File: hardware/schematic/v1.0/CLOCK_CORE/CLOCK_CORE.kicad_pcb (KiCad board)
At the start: 4 copper layers, 70 x 70 mm, 137 parts, among them CN1 LAIL-PHC2_54-2P-01-XH-L, J1 Conn_Coaxial, J3 Conn_01x04_Socket, U1 OCXO_20x20mm, U2 OCXO_25.4x25.4mm, U3 TPS7A5201RPSR, U4 TPS7A5201RPSR, U5 LMK5B12204, U6 REF5040

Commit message: pcb update
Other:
- board text added: "+5V"
- board text added: "GND"

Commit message: pcb update
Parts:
- R20: value DNP -> 0
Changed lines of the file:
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@@
 			)
 		)
-		(property "Value" "DNP"
+		(property "Value" "0"
 			(at 0 1.65 0)
 			(layer "F.Fab")
@@
 			)
 		)
-		(attr smd)
+		(attr smd dnp)
 		(duplicate_pad_numbers_are_jumpers no)
 		(fp_line
@@
 			)
 		)
-		(attr smd)
+		(attr smd dnp)
 		(duplicate_pad_numbers_are_jumpers no)
 		(fp_rect

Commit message: sch and pcb update
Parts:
- C1, C10, C11, C13, C15, C19, C2, C20, C21, C25, C26, C27, C28, C29, C3, C30, C31, C32, C33, C34, C35, C36, C37, C38, C39, C4, C40, C41, C42, C43, C44, C45, C46, C47, C48, C49, C5, C50, C51, C52, C53, C54, C55, C59, C6, C7, C8, C9: footprint Capacitor_SMD:C_0402_1005Metric -> CLOCK_CORE:C_0402_1005Metric
- C12, C14, C18, C56, C57, C58: footprint Capacitor_SMD:C_0603_1608Metric -> CLOCK_CORE:C_0603_1608Metric
- C16, C17, C23, C24: footprint Capacitor_SMD:C_0805_2012Metric -> CLOCK_CORE:C_0805_2012Metric
- C22: footprint JLCImport:TAJB107M010RNJ -> CLOCK_CORE:TAJB107M010RNJ
- CN1: footprint JLCImport:LAIL-PHC2_54-2P-01-XH-L -> CLOCK_CORE:LAIL-PHC2_54-2P-01-XH-L
- D1, D2, D3, D4, D5: footprint LED_SMD:LED_0603_1608Metric -> CLOCK_CORE:LED_0603_1608Metric
- F1: footprint JLCImport:BSMD1206C-1300T -> CLOCK_CORE:BSMD1206C-1300T
- FB1, FB2, FB3, FB4, FB5, FB6, FB7: footprint Inductor_SMD:L_0603_1608Metric -> CLOCK_CORE:L_0603_1608Metric
- H1: footprint JLCImport:HX_PH254-01-03-Z-L11_5_PCB_PIN_HEADER -> CLOCK_CORE:HX_PH254-01-03-Z-L11_5_PCB_PIN_HEADER
- H2, H3, H4, H5: footprint MountingHole:MountingHole_3.2mm_M3_Pad -> CLOCK_CORE:MountingHole_3.2mm_M3_Pad
- J1: footprint Connector_Coaxial:SMA_Amphenol_132134-11_Vertical -> CLOCK_CORE:SMA_Amphenol_132134-11_Vertical
- J3: footprint Connector_PinHeader_2.54mm:PinHeader_1x04_P2.54mm_Vertical -> CLOCK_CORE:PinHeader_1x04_P2.54mm_Vertical
- R1, R10, R11, R12, R13, R14, R16, R17, R18, R2, R21, R22, R23, R24, R3, R30, R31, R32, R33, R34, R35, R36, R37, R38, R4, R5, R6, R7, R8, R9: footprint Resistor_SMD:R_0402_1005Metric -> CLOCK_CORE:R_0402_1005Metric
- R15: footprint Counter:3296W-1-103_C48997937 -> CLOCK_CORE:3296W-1-103_C48997937
- R19, R20, R39: footprint Resistor_SMD:R_0805_2012Metric -> CLOCK_CORE:R_0805_2012Metric
- R25, R26, R27, R28, R29: footprint Resistor_SMD:R_0603_1608Metric -> CLOCK_CORE:R_0603_1608Metric
- RF1, RF10, RF2, RF3, RF4, RF5, RF6, RF7, RF8, RF9: footprint JLCImport:KH-IPEX-K501-29 -> CLOCK_CORE:KH-IPEX-K501-29
- TP1, TP2: footprint TestPoint:TestPoint_Pad_D1.0mm -> CLOCK_CORE:TestPoint_Pad_D1.0mm
- U1: footprint JLCImport:OCXO_20x20mm -> CLOCK_CORE:OCXO_20x20mm
- U2: footprint JLCImport:DOPFITKR2-10M -> CLOCK_CORE:DOPFITKR2-10M
- U3, U4: footprint JLCImport:TPS7A5201RPSR -> CLOCK_CORE:TPS7A5201RPSR
- U5: footprint Package_DFN_QFN:VQFN-48-1EP_7x7mm_P0.5mm_EP5.15x5.15mm_ThermalVias -> CLOCK_CORE:VQFN-48-1EP_7x7mm_P0.5mm_EP5.15x5.15mm_ThermalVias
- U6: footprint JLCImport:REF5040 -> CLOCK_CORE:REF5040

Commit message: sch and pcb update
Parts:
- R12, R3, R6, R9: value DNP -> 100
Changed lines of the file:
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@@
 			)
 		)
-		(property "Value" "DNP"
+		(property "Value" "100"
 			(at 0 1.17 90)
 			(layer "F.Fab")
@@
 			)
 		)
-		(property "Value" "DNP"
+		(property "Value" "100"
 			(at 0 1.17 90)
 			(layer "F.Fab")
@@
 			)
 		)
-		(property "Value" "DNP"
+		(property "Value" "100"
 			(at 0 1.17 90)
 			(layer "F.Fab")
@@
 			)
 		)
-		(property "Value" "DNP"
+		(property "Value" "100"
 			(at 0 1.17 90)
 			(layer "F.Fab")

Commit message: pcb update
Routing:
- net GND: track 111.1 -> 115.1 mm
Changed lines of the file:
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@@
+	)
+	(segment
+		(start 136.89 98.89)
+		(end 135.56 98.89)
+		(width 0.3)
+		(layer "F.Cu")
+		(net "GND")
 	)
 	(segment
@@
 	)
 	(segment
-		(start 136.89 98.89)
-		(end 136.89 99.64)
-		(width 0.3)
-		(layer "F.Cu")
-		(net "GND")
-	)
-	(segment
 		(start 179.2125 115.325)
 		(end 179.2125 116.15)
@@
 	)
 	(segment
+		(start 126.16 61.87)
+		(end 126.16 62.89)
+		(width 0.2)
+		(layer "F.Cu")
+		(net "GND")
+	)
+	(segment
 		(start 118.5 113.98)
 		(end 118.5 113.23)
@@
 	)
 	(segment
-		(start 126.1621 64.81)
-		(end 126.1621 64.06)
+		(start 126.1621 62.8921)
+		(end 126.1621 64.81)
 		(width 0.2)
 		(layer "F.Cu")
@@
 	)
 	(segment
+		(start 126.16 62.89)
+		(end 126.1621 62.8921)
+		(width 0.2)
+		(layer "F.Cu")
+		(net "GND")
+	)
+	(segment
 		(start 118.5 94.52)
 		(end 118.5 95.27)
@@
 	)
 	(via
-		(at 136.89 99.64)
+		(at 135.56 98.89)
 		(size 0.6)
 		(drill 0.3)
@@
 	)
 	(via
-		(at 126.1621 64.06)
-		(size 0.6)
-		(drill 0.3)
-		(layers "F.Cu" "B.Cu")
-		(net "GND")
-	)
-	(via
-		(at 150.1375 93.2975)
+		(at 126.16 61.87)
+		(size 0.6)
+		(drill 0.3)
+		(layers "F.Cu" "B.Cu")
+		(net "GND")
+	)
+	(via
+		(at 150.14 92.07)
 		(size 0.6)
 		(drill 0.3)
@@
 	)
 	(segment
+		(start 150.1375 94.0975)
+		(end 150.1375 92.0725)
+		(width 0.3)
+		(layer "B.Cu")
+		(net "GND")
+	)
+	(segment
 		(start 146.16 94.08)
 		(end 145.26 94.08)
@@
 	)
 	(segment
-		(start 150.1375 94.0975)
-		(end 150.1375 93.2975)
+		(start 150.1375 92.0725)
+		(end 150.14 92.07)
 		(width 0.3)
 		(layer "B.Cu")

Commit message: sch and pcb update
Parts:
- added R40: 0, CLOCK_CORE:R_0402_1005Metric, F.Cu at (165.4, 102.9)
- added R41: 0, CLOCK_CORE:R_0402_1005Metric, F.Cu at (165.4, 104.9)
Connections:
- R13 pad 1: OCXO_OUT -> OCXO_FR
- R30 pad 1: OCXO_OUT -> OCXO_FR
- U2 pad 1: OCXO_OUT -> OCXO_FR
- U5 pad 31: OCXO_OUT -> /LMK5B12204/OCXO_OUT
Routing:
- net OCXO_OUT: track 21.8 -> 0.00 mm
- net (no net): track 0.00 -> 21.8 mm

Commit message: sch and pcb update
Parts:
- moved R40 20.6 mm to (146.2, 95.6), turned to -90 degrees
- moved R41 19.8 mm to (147.6, 96.0)
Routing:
- net (no net): track 21.8 -> 0.00 mm
- net OCXO_FR: track 0.00 -> 16.7 mm
- net /LMK5B12204/OCXO_OUT: track 0.00 -> 5.00 mm
- net GND: track 115.1 -> 115.7 mm, vias 88 -> 87
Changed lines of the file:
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@@
 	(footprint "CLOCK_CORE:R_0402_1005Metric"
 		(layer "F.Cu")
-		(at 165.395 102.905)
+		(at 146.15 95.550001 -90)
 		(descr "Resistor SMD 0402 (1005 Metric), square (rectangular) end terminal, IPC-7351 nominal, (Body size source: IPC-SM-782 page 72, https://www.pcb-3d.com/wordpress/wp-content/uploads/ipc-sm-782a_amendment_1_and_2.pdf)")
 		(tags "resistor")
 		(property "Reference" "R40"
-			(at 0 -1.17 0)
+			(at 0.020001 -0.97 90)
 			(layer "F.SilkS")
+			(hide yes)
 			(effects
 				(font
-					(size 1 1)
-					(thickness 0.15)
+					(size 0.5 0.5)
+					(thickness 0.1)
+					(bold yes)
 				)
 			)
 		)
 		(property "Value" "0"
-			(at 0 1.17 0)
+			(at 0 1.17 90)
 			(layer "F.Fab")
+			(hide yes)
 			(effects
 				(font
@@
 		)
 		(property "Datasheet" ""
-			(at 0 0 0)
+			(at 0 0 90)
 			(layer "F.Fab")
 			(hide yes)
@@
 		)
 		(property "Description" ""
-			(at 0 0 0)
+			(at 0 0 90)
 			(layer "F.Fab")
 			(hide yes)
@@
 		)
 		(property "KiLib_Generator" "SMD_2terminal_chip_molded"
-			(at 0 0 0)
+			(at 0 0 90)
 			(layer "F.SilkS")
 			(hide yes)
@@
 		(duplicate_pad_numbers_are_jumpers no)
 		(fp_line
-			(start -0.153641 -0.38)
-			(end 0.153641 -0.38)
+			(start -0.153641 0.38)
+			(end 0.153641 0.38)
 			(stroke
 				(width 0.12)
@@
 		)
 		(fp_line
-			(start -0.153641 0.38)
-			(end 0.153641 0.38)
+			(start -0.153641 -0.38)
+			(end 0.153641 -0.38)
 			(stroke
 				(width 0.12)
@@
 			(layer "F.SilkS")
 		)
-		(fp_rect
-			(start -0.93 -0.47)
-			(end 0.93 0.47)
+		(fp_poly
+			(pts
+				(xy -0.93 -0.47) (xy 0.93 -0.47) (xy 0.93 0.47) (xy -0.93 0.47)
+			)
 			(stroke
 				(width 0.05)
@@
 			(layer "F.CrtYd")
 		)
-		(fp_rect
-			(start -0.525 -0.27)
-			(end 0.525 0.27)
+		(fp_poly
+			(pts
+				(xy -0.525 -0.27) (xy 0.525 -0.27) (xy 0.525 0.27) (xy -0.525 0.27)
+			)
 			(stroke
 				(width 0.1)
@@
 		)
 		(fp_text user "${REFERENCE}"
-			(at 0 0 0)
+			(at 0 0 90)
 			(layer "F.Fab")
 			(effects
@@
 		)
 		(pad "1" smd roundrect
-			(at -0.51 0)
+			(at -0.509999 0 270)
 			(size 0.54 0.64)
 			(layers "F.Cu" "F.Mask" "F.Paste")
@@
 		)
 		(pad "2" smd roundrect
-			(at 0.51 0)
+			(at 0.509999 0 270)
 			(size 0.54 0.64)
 			(layers "F.Cu" "F.Mask" "F.Paste")
@@
 	(footprint "CLOCK_CORE:R_0402_1005Metric"
 		(layer "F.Cu")
-		(at 165.395 104.895)
+		(at 147.649999 96.040002)
 		(descr "Resistor SMD 0402 (1005 Metric), square (rectangular) end terminal, IPC-7351 nominal, (Body size source: IPC-SM-782 page 72, https://www.pcb-3d.com/wordpress/wp-content/uploads/ipc-sm-782a_amendment_1_and_2.pdf)")
 		(tags "resistor")
 		(property "Reference" "R41"
-			(at 0 -1.17 0)
+			(at 0.000001 -1.04 0)
 			(layer "F.SilkS")
+			(hide yes)
 			(effects
 				(font
-					(size 1 1)
-					(thickness 0.15)
+					(size 0.5 0.5)
+					(thickness 0.1)
+					(bold yes)
 				)
 			)
@@
 			(at 0 1.17 0)
 			(layer "F.Fab")
+			(hide yes)
 			(effects
 				(font
@@
 			)
 		)
-		(attr smd)
+		(attr smd dnp)
 		(duplicate_pad_numbers_are_jumpers no)
 		(fp_line
@@
 			(layer "F.SilkS")
 		)
-		(fp_rect
-			(start -0.93 -0.47)
-			(end 0.93 0.47)
+		(fp_poly
+			(pts
+				(xy -0.93 -0.47) (xy 0.93 -0.47) (xy 0.93 0.47) (xy -0.93 0.47)
+			)
 			(stroke
 				(width 0.05)
@@
 			(layer "F.CrtYd")
 		)
-		(fp_rect
-			(start -0.525 -0.27)
-			(end 0.525 0.27)
+		(fp_poly
+			(pts
+				(xy -0.525 -0.27) (xy 0.525 -0.27) (xy 0.525 0.27) (xy -0.525 0.27)
+			)
 			(stroke
 				(width 0.1)
@@
 		)
 		(pad "1" smd roundrect
-			(at -0.51 0)
+			(at -0.509999 0)
 			(size 0.54 0.64)
 			(layers "F.Cu" "F.Mask" "F.Paste")
@@
 		)
 		(pad "2" smd roundrect
-			(at 0.51 0)
+			(at 0.509999 0)
 			(size 0.54 0.64)
 			(layers "F.Cu" "F.Mask" "F.Paste")
@@
 	)
 	(segment
-		(start 146.15 93.11)
-		(end 146.15 100.075)
-		(width 0.15)
-		(locked yes)
-		(layer "F.Cu")
-		(net "")
-	)
-	(segment
-		(start 139.01008 92.13)
-		(end 145.17 92.13)
-		(width 0.15)
-		(locked yes)
-		(layer "F.Cu")
-		(net "")
-	)
-	(segment
-		(start 145.17 92.13)
-		(end 146.15 93.11)
-		(width 0.15)
-		(locked yes)
-		(layer "F.Cu")
-		(net "")
-	)
-	(segment
-		(start 137.407 90.52692)
-		(end 139.01008 92.13)
-		(width 0.15)
-		(locked yes)
-		(layer "F.Cu")
-		(net "")
-	)
-	(segment
-		(start 137.407 90.52692)
-		(end 135.990079 89.109999)
-		(width 0.15)
-		(locked yes)
-		(layer "B.Cu")
-		(net "")
-	)
-	(segment
-		(start 135.99 89.109999)
-		(end 135.99 88.66)
-		(width 0.15)
-		(locked yes)
-		(layer "B.Cu")
-		(net "")
-	)
-	(segment
-		(start 137.42392 90.51)
-		(end 137.407 90.52692)
-		(width 0.15)
-		(layer "B.Cu")
-		(net "")
-	)
-	(segment
-		(start 135.990079 89.109999)
-		(end 135.99 89.109999)
-		(width 0.15)
-		(locked yes)
-		(layer "B.Cu")
-		(net "")
-	)
-	(segment
-		(start 139.930001 90.51)
-		(end 137.42392 90.51)
-		(width 0.15)
-		(locked yes)
-		(layer "B.Cu")
-		(net "")
-	)
-	(segment
 		(start 150.584751 104.6715)
 		(end 150.493751 104.7625)
@@
 	)
 	(segment
+		(start 148.17 97.02)
+		(end 147.47 97.02)
+		(width 0.3)
+		(layer "F.Cu")
+		(net "GND")
+	)
+	(segment
 		(start 136.89 98.89)
 		(end 135.56 98.89)
@@
 	)
 	(segment
+		(start 148.17 97.02)
+		(end 148.17 96.050004)
+		(width 0.3)
+		(layer "F.Cu")
+		(net "GND")
+	)
+	(segment
 		(start 130.19 88.67)
 		(end 130.19 89.42)
@@
 	)
 	(segment
+		(start 147.47 97.02)
+		(end 147.41 96.96)
+		(width 0.3)
+		(layer "F.Cu")
+		(net "GND")
+	)
+	(segment
 		(start 179.2125 115.325)
 		(end 179.2125 116.15)
@@
 	)
 	(segment
+		(start 148.17 96.050004)
+		(end 148.159998 96.040002)
+		(width 0.3)
+		(layer "F.Cu")
+		(net "GND")
+	)
+	(segment
 		(start 126.21 87.371)
 		(end 126.21 88.171)
@@
 	)
 	(segment
-		(start 148.17 97.02)
-		(end 148.17 95.87)
-		(width 0.3)
-		(layer "F.Cu")
-		(net "GND")
-	)
-	(segment
 		(start 161.56 81.12)
 		(end 162.71 81.12)
@@
 	)
 	(via
-		(at 148.17 95.87)
-		(size 0.6)
-		(drill 0.3)
-		(layers "F.Cu" "B.Cu")
-		(net "GND")
-	)
-	(via
 		(at 178.2 117.5)
 		(size 0.6)
@@
 	)
 	(segment
+		(start 146.15 96.06)
+		(end 147.119998 96.06)
+		(width 0.15)
+		(locked yes)
+		(layer "F.Cu")
+		(net "/LMK5B12204/OCXO_OUT")
+	)
+	(segment
+		(start 147.119998 95.949998)
+		(end 147.13 95.96)
+		(width 0.15)
+		(layer "F.Cu")
+		(net "/LMK5B12204/OCXO_OUT")
+	)
+	(segment
+		(start 146.15 96.06)
+		(end 146.15 100.075)
+		(width 0.15)
+		(locked yes)
+		(layer "F.Cu")
+		(net "/LMK5B12204/OCXO_OUT")
+	)
+	(segment
 		(start 145.15 100.075)
 		(end 145.15 98.94)
@@
 	)
 	(segment
+		(start 139.01008 92.13)
+		(end 145.17 92.13)
+		(width 0.15)
+		(locked yes)
+		(layer "F.Cu")
+		(net "OCXO_FR")
+	)
+	(segment
+		(start 146.15 93.11)
+		(end 146.15 95.040002)
+		(width 0.15)
+		(locked yes)
+		(layer "F.Cu")
+		(net "OCXO_FR")
+	)
+	(segment
+		(start 137.407 90.52692)
+		(end 139.01008 92.13)
+		(width 0.15)
+		(locked yes)
+		(layer "F.Cu")
+		(net "OCXO_FR")
+	)
+	(segment
+		(start 145.17 92.13)
+		(end 146.15 93.11)
+		(width 0.15)
+		(locked yes)
+		(layer "F.Cu")
+		(net "OCXO_FR")
+	)
+	(segment
+		(start 137.407 90.52692)
+		(end 135.990079 89.109999)
+		(width 0.15)
+		(locked yes)
+		(layer "B.Cu")
+		(net "OCXO_FR")
+	)
+	(segment
+		(start 135.99 89.109999)
+		(end 135.99 88.66)
+		(width 0.15)
+		(locked yes)
+		(layer "B.Cu")
+		(net "OCXO_FR")
+	)
+	(segment
+		(start 137.42392 90.51)
+		(end 137.407 90.52692)
+		(width 0.15)
+		(layer "B.Cu")
+		(net "OCXO_FR")
+	)
+	(segment
+		(start 135.990079 89.109999)
+		(end 135.99 89.109999)
+		(width 0.15)
+		(locked yes)
+		(layer "B.Cu")
+		(net "OCXO_FR")
+	)
+	(segment
+		(start 139.930001 90.51)
+		(end 137.42392 90.51)
+		(width 0.15)
+		(locked yes)
+		(layer "B.Cu")
+		(net "OCXO_FR")
+	)
+	(segment

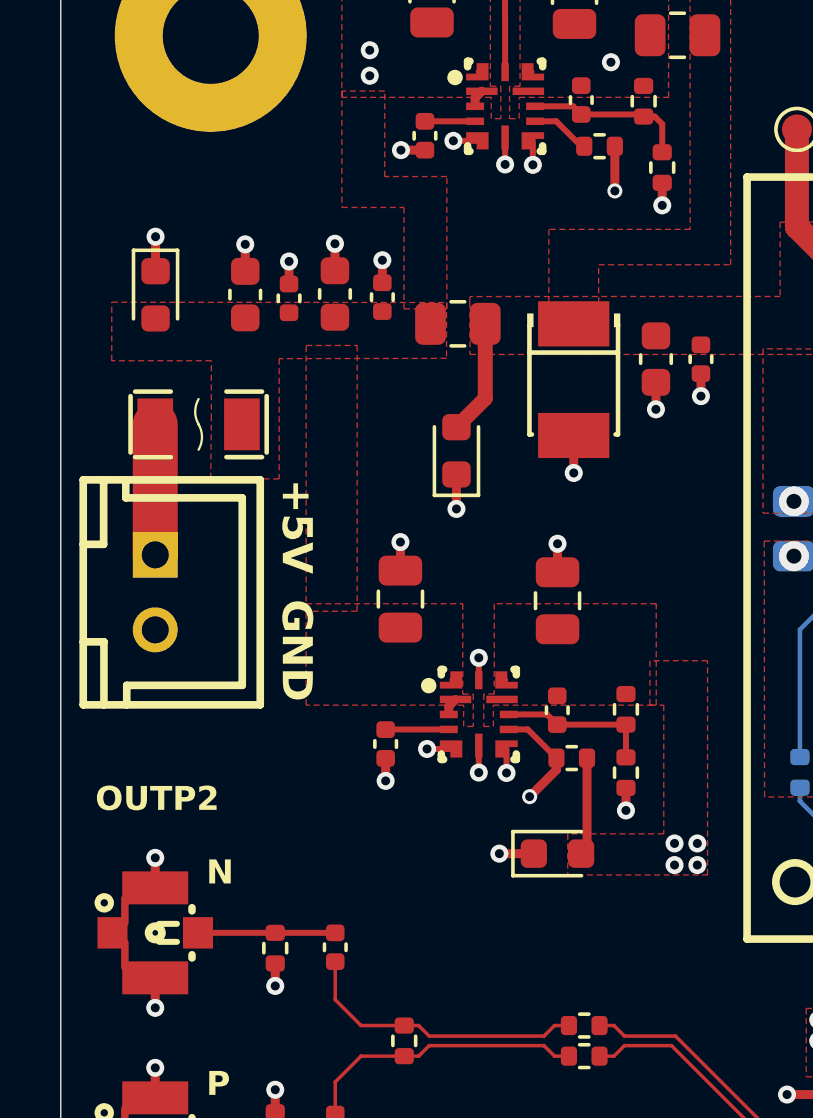
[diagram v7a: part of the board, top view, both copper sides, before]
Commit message: Add a current-limiting resistor, sch and pcb update
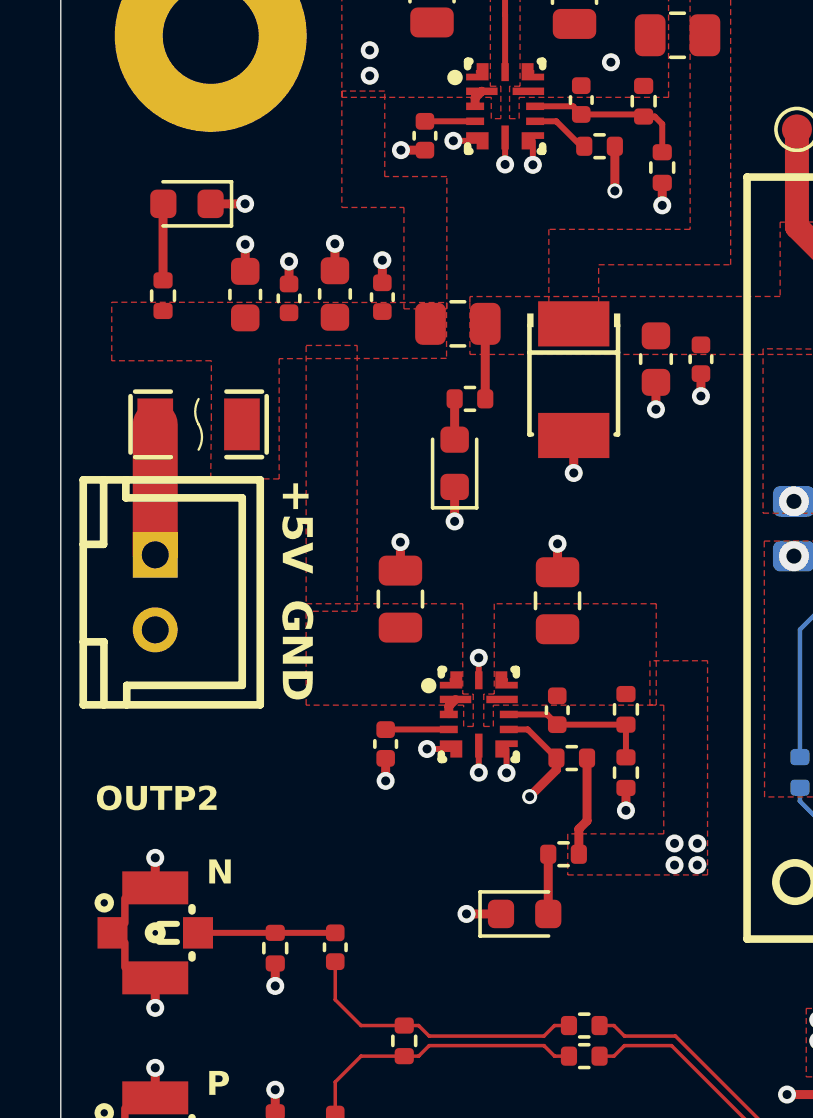
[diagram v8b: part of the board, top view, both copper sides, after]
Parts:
- added R42: 2.2K, CLOCK_CORE:R_0402_1005Metric, F.Cu at (125.0, 75.7)
- added R43: 2.2K, CLOCK_CORE:R_0402_1005Metric, F.Cu at (128.1, 90.9)
- added R46: 2.2K, CLOCK_CORE:R_0402_1005Metric, F.Cu at (114.8, 72.3)
- moved D3 3.21 mm to (115.6, 69.2), turned to 180 degrees
- moved D5 2.29 mm to (126.8, 92.9)
- moved D4 0.42 mm to (124.5, 77.8)
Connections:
- D3 pad 2: +5V -> Net-(D3-A)
- D4 pad 2: OCXO_VCC -> Net-(D4-A)
- D5 pad 2: +3.3V -> Net-(D5-A)
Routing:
- net Net-(D3-A): track 0.00 -> 2.55 mm
- net Net-(D5-A): track 0.00 -> 1.99 mm
- net Net-(D4-A): track 0.00 -> 1.36 mm
- net OCXO_VCC: track 9.24 -> 7.90 mm
- net /LMK5B12204/PDN: track 96.9 -> 97.4 mm
